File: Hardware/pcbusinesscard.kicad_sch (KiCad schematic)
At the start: 73 parts, among them J1 Conn_01x04_Pin, J10 USB_C_Receptacle_USB2.0, J2 Micro_SD_Card, J3 Conn_01x04_Pin, J4 Conn_01x03, SW1 ESC, SW2 `, SW3 1, SW4 2, SW98 SW_Push, U1 nRF52840, U2 24AA025E-OT, U3 24AA025E-OT, U4 24AA025E-OT, U5 BQ24090DGQ, Y1 32.768kHz, Y3 32Mhz

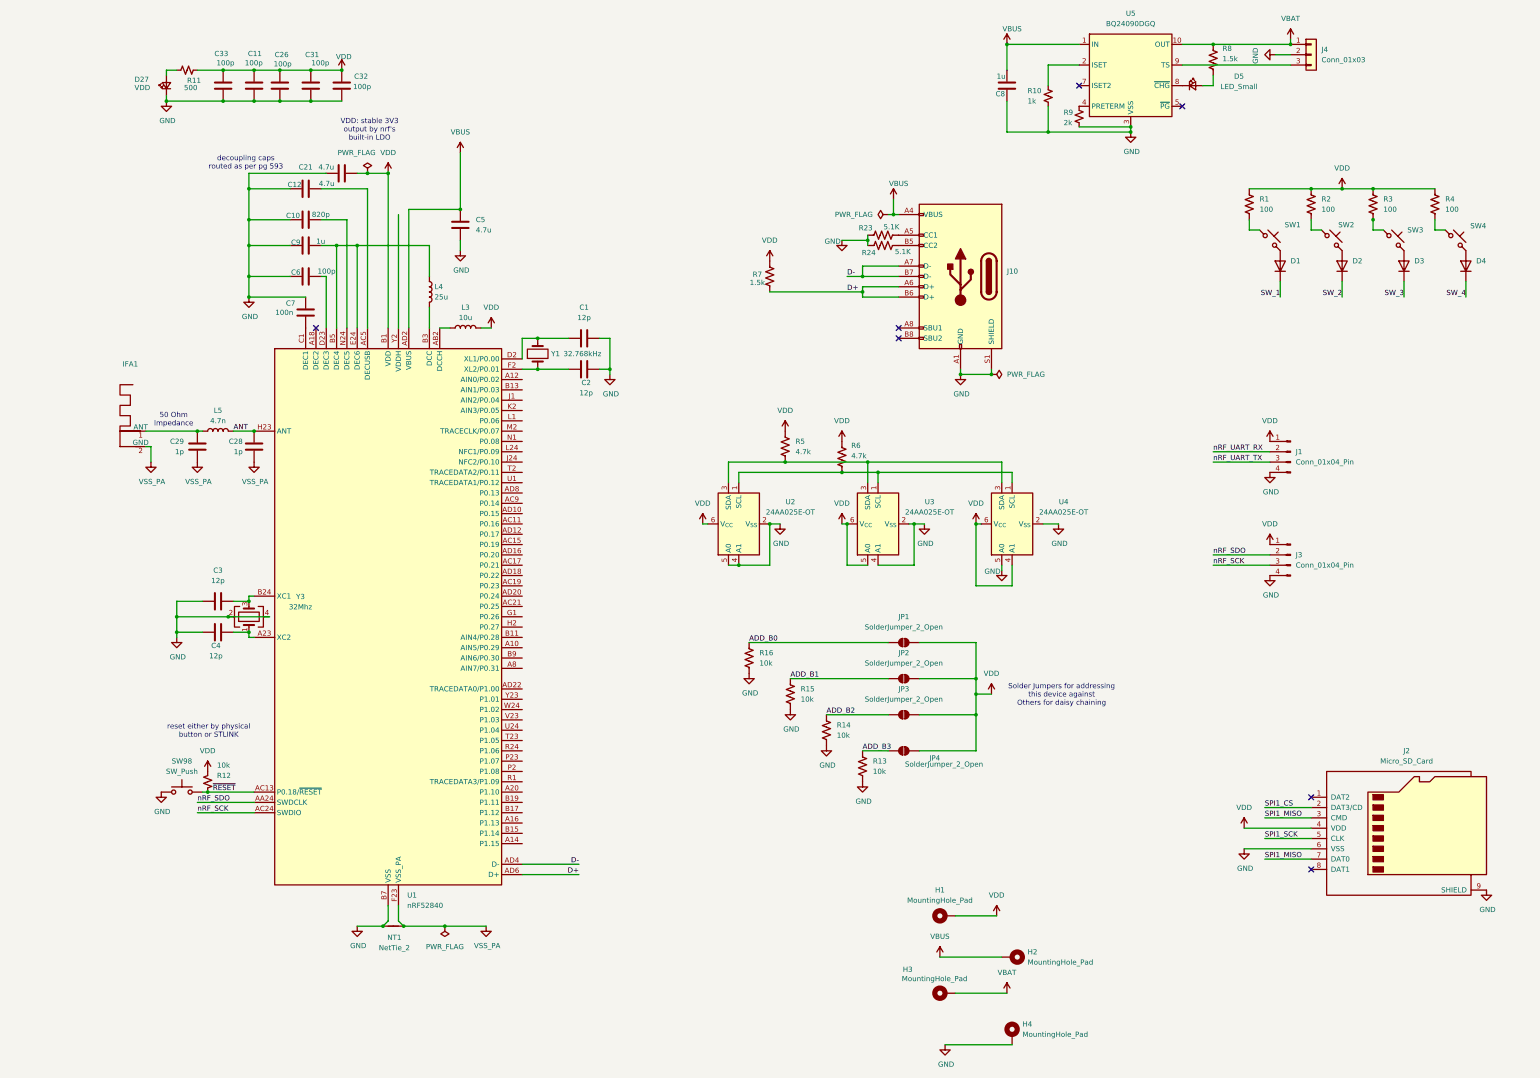
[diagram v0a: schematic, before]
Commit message: Overhaul entire design with RP2040
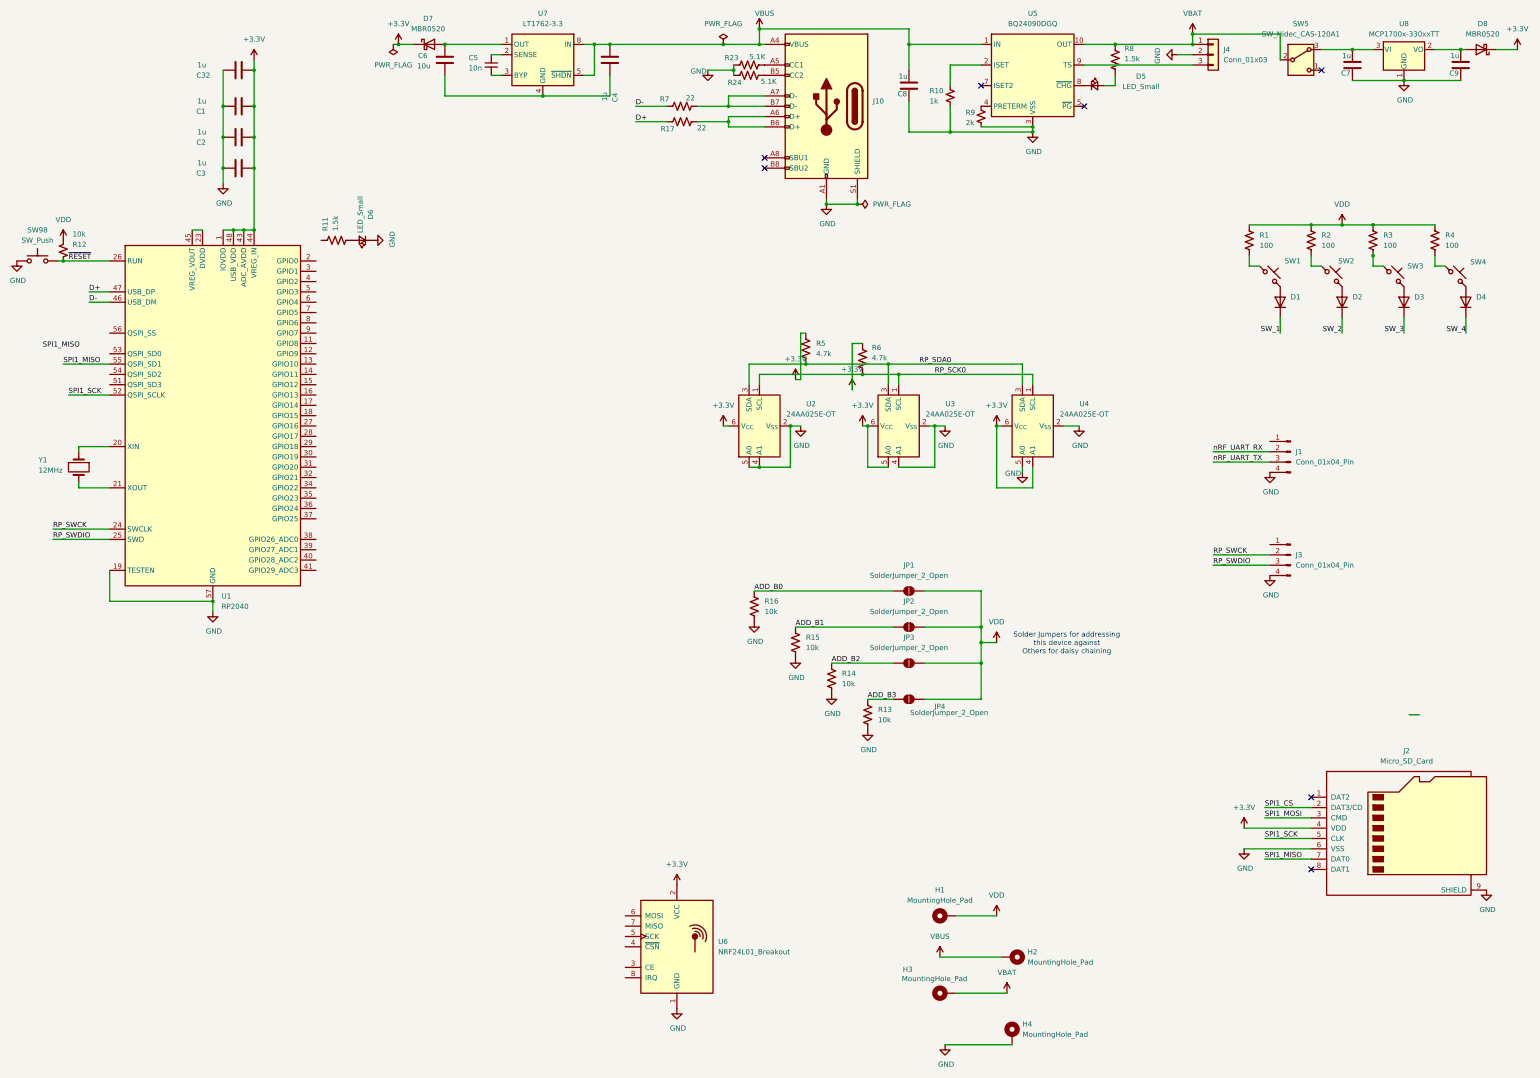
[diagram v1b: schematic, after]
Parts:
- removed C10: 820p, Capacitor_SMD:C_0603_1608Metric, symbol Device:C
- removed C11, C26, C31, C33: 100p, Capacitor_SMD:C_0603_1608Metric, symbol Device:C
- removed C12, C21, C5: 4.7u, Capacitor_SMD:C_0805_2012Metric, symbol Device:C
- removed C28, C29: 1p, Capacitor_SMD:C_0402_1005Metric, symbol Device:C
- removed D27: VDD, LED_SMD:LED_0402_1005Metric, symbol Device:LED_Small
- removed IFA1: ~, RF_Antenna:Texas_SWRA117D_2.4GHz_Right, symbol Custom_sym:IFA
- removed L3: 10u, Inductor_SMD:L_0402_1005Metric, symbol Device:L
- removed L4: 25u, Inductor_SMD:L_0402_1005Metric, symbol Device:L
- removed L5: 4.7n, Inductor_SMD:L_0402_1005Metric, symbol Device:L
- removed NT1: NetTie_2, NetTie:NetTie-2_SMD_Pad2.0mm, symbol Device:NetTie_2
- removed R11: 500, Resistor_SMD:R_0603_1608Metric, symbol Device:R_Small_US
- removed U1: nRF52840, Package_DFN_QFN:Nordic_AQFN-73-1EP_7x7mm_P0.5mm, symbol MCU_Nordic:nRF52840
- removed Y3: 32Mhz, Crystal:Crystal_SMD_2016-4Pin_2.0x1.6mm, symbol Device:Crystal_GND24
- added C5: 10n, Capacitor_SMD:C_0603_1608Metric, symbol Device:C_Small
- added D6: LED_Small, LED_THT:LED_D5.0mm, symbol Device:LED_Small
- added D7, D8: MBR0520, Diode_SMD:D_SOD-123, symbol Diode:MBR0520
- added R11: 1.5k, Resistor_SMD:R_0603_1608Metric, symbol Device:R_US
- added R17: 22, Resistor_SMD:R_0603_1608Metric, symbol Device:R_US
- added SW5: SW_Nidec_CAS-120A1, Button_Switch_SMD:Nidec_Copal_CAS-120A, symbol Switch:SW_Nidec_CAS-120A1
- added U1: RP2040, Package_DFN_QFN:QFN-56-1EP_7x7mm_P0.4mm_EP3.2x3.2mm, symbol MCU_RaspberryPi:RP2040
- added U6: NRF24L01_Breakout, RF_Module:nRF24L01_Breakout, symbol RF:NRF24L01_Breakout
- added U7: LT1762-3.3, Package_SO:MSOP-8_3x3mm_P0.65mm, symbol Regulator_Linear:LT1762-3.3
- added U8: MCP1700x-330xxTT, Package_TO_SOT_SMD:SOT-23, symbol Regulator_Linear:MCP1700x-330xxTT
- C1, C2, C3, C4: value 12p -> 1u; footprint Capacitor_SMD:C_0402_1005Metric -> Capacitor_SMD:C_0603_1608Metric; LCSC C1547 -> C14858
- C32: value 100p -> 1u
- C6: value 100p -> 10u
- C7: value 100n -> 1u; LCSC C14663 -> C15849
- J1, J3: footprint Connector_Card:microSD_HC_Molex_47219-2001 -> Connector_JST:JST_PH_B4B-PH-K_1x04_P2.00mm_Vertical
- R7: value 1.5k -> 22; LCSC C22843 -> C23186
- SW1, SW2, SW3, SW4: footprint ScottoKeebs_Hotswap:Hotswap_MX_1.00u -> ScottoKeebs_MX:MX_PCB_1.00u
- Y1: value 32.768kHz -> 12MHz; footprint Crystal:Crystal_SMD_3215-2Pin_3.2x1.5mm -> Crystal:Crystal_SMD_5032-2Pin_5.0x3.2mm; LCSC C32346 -> (none)
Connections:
- net D+: now also R17.1, U1.47 (USB_DP); no longer J10.A6 (D+), J10.B6 (D+), R7.2
- net D-: now also R7.1, U1.46 (USB_DM); no longer J10.A7 (D-), J10.B7 (D-)
- net GND: now also C32.1, D6.1 (K), U1.19 (TESTEN), U1.57 (GND), U6.1 (GND), U8.1 (GND); no longer C32.2, C4.1, C6.2
- net SPI1_MISO: now also U1.55 (QSPI_SD1); no longer J2.3 (CMD)
- net SPI1_SCK: now also U1.52 (QSPI_SCLK)
- net VBAT: now also SW5.2 (B)
- net VBUS: now also C4.2, U7.5 (~{SHDN}), U7.8 (IN)
- net VDD: no longer C32.1, J1.1 (Pin_1), J2.4 (VDD), J3.1 (Pin_1), R5.1, R6.1, R7.1, U2.6 (V_{CC}), U3.5 (A0), U3.6 (V_{CC}), U4.4 (A1), U4.6 (V_{CC})
- net ~{RESET}: now also U1.26 (RUN)
- net +3.3V: now reaches C3.2
- net +3.3V: now also C1.2, C2.2, C32.2, J2.4 (VDD), R5.1, R6.1, U2.6 (V_{CC}), U3.5 (A0), U3.6 (V_{CC}), U4.4 (A1), U4.6 (V_{CC}), D7.1 (K), D8.1 (K), U1.1 (IOVDD), U1.10 (IOVDD), U1.22 (IOVDD), U1.33 (IOVDD), U1.42 (IOVDD), U1.43 (ADC_AVDD), U1.44 (VREG_IN), U1.48 (USB_VDD), U1.49 (IOVDD), U6.2 (VCC)
- net RP_SDA0: now reaches R5.2, U2.3 (SDA), U3.3 (SDA), U4.3 (SDA)
- net at C9.1: now also D8.2 (A), U8.2 (VO)
- net at C7.1: now also SW5.3 (A), U8.3 (VI)
- net at Y1.2: now also U1.21 (XOUT); no longer C1.2
- net at C6.1: now also C4.1, U7.4 (GND)
- net at Y1.1: now also U1.20 (XIN); no longer C2.2
- net RP_SCK0: now reaches R6.2, U2.1 (SCL), U3.1 (SCL), U4.1 (SCL)
- net nRF_SCK renamed RP_SWDIO
- net RP_SWDIO: now also U1.25 (SWD)
- net nRF_SDO renamed RP_SWCK
- net RP_SWCK: now also U1.24 (SWCLK)
- new net: C6.2, D7.2 (A), U7.1 (OUT)
- new net: C5.1, U7.2 (SENSE)
- new net: C5.2, U7.3 (BYP)
- new net: D6.2 (A), R11.2
- new net: U1.23 (DVDD), U1.45 (VREG_VOUT), U1.50 (DVDD)
- new net: J10.A7 (D-), J10.B7 (D-), R7.2
- new net: J10.A6 (D+), J10.B6 (D+), R17.2
- new net SPI1_MOSI: J2.3 (CMD)
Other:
- note removed: "50 Ohm Impedance"
- note removed: "VDD: stable 3V3 output by nrf's built-in LDO"
- note removed: "decoupling caps routed as per pg 593"
- note removed: "reset either by physical button or STLINK"
- moved on the sheet: C32, C8, D1, D2, D3, D4, D5, J10, J4, JP1, JP2, JP3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

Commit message: adding to layout
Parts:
- added C10: 1u, Capacitor_SMD:C_0603_1608Metric, symbol Device:C
- added D10, D9: LED_Small, LED_SMD:LED_0805_2012Metric, symbol Device:LED_Small
- added R18, R19: 1.5k, Resistor_SMD:R_0603_1608Metric, symbol Device:R_US
- C1: value 1u -> 4.7u
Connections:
- net +3.3V: now also H3.1, J1.1 (Pin_1), J3.1 (Pin_1), JP1.2 (B), JP2.2 (B), JP3.2 (B), JP4.2 (B), R1.1, R12.1, R2.1, R3.1, R4.1, C10.2
- net ADD_B0: now also U1.40 (GPIO28_ADC2)
- net ADD_B1: now also U1.39 (GPIO27_ADC1)
- net ADD_B2: now also U1.38 (GPIO26_ADC0)
- net ADD_B3: now also U1.37 (GPIO25)
- net GND: now also C10.1, D10.1 (K), D9.1 (K)
- net RP_SCK0: now also U1.29 (GPIO18)
- net RP_SDA0: now also U1.30 (GPIO19)
- net SPI1_CS: now also U1.12 (GPIO9)
- net SPI1_MISO: now also U1.15 (GPIO12); no longer U1.55 (QSPI_SD1)
- net SPI1_MOSI: now also U1.9 (GPIO7)
- net SPI1_SCK: now also U1.13 (GPIO10); no longer U1.52 (QSPI_SCLK)
- net SW_1: now also U1.34 (GPIO22)
- net SW_2: now also U1.36 (GPIO24)
- net SW_3: now also U1.31 (GPIO20)
- net SW_4: now also U1.35 (GPIO23)
- net VBAT: now also H2.1; no longer H3.1
- net VBUS: now also H1.1, R11.1; no longer H2.1
- net d-: now reaches J10.A7 (D-), J10.B7 (D-), R7.2
- net d+: now reaches J10.A6 (D+), J10.B6 (D+), R17.2
- removed net VDD: H1.1, JP1.2 (B), JP2.2 (B), JP3.2 (B), JP4.2 (B), R1.1, R12.1, R2.1, R3.1, R4.1
- new net: D9.2 (A), R18.2
- new net: D10.2 (A), R19.2
- no-connect marks 7 -> 8
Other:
- note added: "MCU"
- note added: "POWER"
- note removed: "Solder Jumpers for addressing this device against Others for daisy chaining"
- moved on the sheet: C1, C2, C3, C32, C4, C5, C6, C7, C8, C9, D1, D2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

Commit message: Finish Draft
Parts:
- removed D7, D8: MBR0520, Diode_SMD:D_SOD-123, symbol Diode:MBR0520
- added C11: 1u, Capacitor_SMD:C_0603_1608Metric, symbol Device:C
- added J5: Conn_ST_STDC14, Connector_PinHeader_1.27mm:PinHeader_2x07_P1.27mm_Vertical, symbol Connector:Conn_ST_STDC14
- added R20: 1.5k, Resistor_SMD:R_0603_1608Metric, symbol Device:R_US
- added R21, R22: 10k, Resistor_SMD:R_0603_1608Metric, symbol Device:R_US
- added TP1, TP2, TP3, TP4, TP5: TestPoint, TestPoint:TestPoint_Keystone_5010-5014_Multipurpose, symbol Connector:TestPoint
- added U9: TPS2116DRL, Package_TO_SOT_SMD:SOT-583-8, symbol Power_Management:TPS2116DRL
- J3: footprint Connector_JST:JST_PH_B4B-PH-K_1x04_P2.00mm_Vertical -> Connector_PinHeader_2.54mm:PinHeader_1x04_P2.54mm_Vertical
- J4: footprint Connector_JST:JST_GH_SM03B-GHS-TB_1x03-1MP_P1.25mm_Horizontal -> Connector_JST:JST_ZH_B3B-ZR_1x03_P1.50mm_Vertical
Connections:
- net +3.3V: now also C11.2, J5.3 (VCC), U9.2 (VOUT), U9.7 (VOUT)
- net GND: now also C4.1, C6.1, U7.4 (GND), C11.1, J5.11 (GNDDetect), J5.5 (GND), J5.7 (GND), R21.2, U9.1 (GND)
- net RP_SCK0: now also TP2.1
- net RP_SDA0: now also TP1.1
- net RP_SWCK: now also J5.6 (JCLK/SWCLK)
- net RP_SWDIO: now also J5.4 (JTMS/SWDIO)
- net SPI1_MISO: now also TP4.1
- net SPI1_MOSI: now also TP5.1
- net SPI1_SCK: now also TP3.1
- net VBAT: now also SW5.1 (C), R22.2
- net nRF_UART_RX: now also J1.3 (Pin_3), U1.28 (GPIO17); no longer J1.2 (Pin_2)
- net nRF_UART_TX: now also J1.2 (Pin_2), U1.27 (GPIO16); no longer J1.3 (Pin_3)
- net ~{RESET}: now also J5.12 (~{RST})
- net VBUS_LDO: now reaches C6.2, U7.1 (OUT)
- net VBUS_LDO: now also R20.1, U9.3 (VIN1), U9.4 (PR1), U9.5 (MODE)
- net status_LED0: now reaches R18.1
- net status_LED0: now also U1.51 (QSPI_SD3)
- net nRF_CE: now reaches U6.3 (CE)
- net nRF_CE: now also U1.2 (GPIO0)
- net SPI0_CSN: now reaches U6.4 (~{CSN})
- net SPI0_CSN: now also U1.3 (GPIO1)
- net SPI0_SCK: now reaches U6.5 (SCK)
- net SPI0_SCK: now also U1.4 (GPIO2)
- net SPI0_MOSI: now reaches U6.6 (MOSI)
- net SPI0_MOSI: now also U1.5 (GPIO3)
- net SPI0_MISO: now reaches U6.7 (MISO)
- net SPI0_MISO: now also U1.6 (GPIO4)
- net nRF_IRQ: now reaches U6.8 (IRQ)
- net nRF_IRQ: now also U1.7 (GPIO5)
- net status_LED1: now reaches R19.1
- net status_LED1: now also U1.52 (QSPI_SCLK)
- net at U1.41 (GPIO29_ADC3): now also R21.1, R22.1
- net VBAT_LDO: now reaches C9.1, U8.2 (VO)
- net VBAT_LDO: now also U9.6 (VIN2)
- new net: R20.2, U9.8 (ST)
- no-connect marks 8 -> 22
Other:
- note added: "redundant header"
- moved on the sheet: C1, C10, C2, C3, C32, C7, C9, D1, D10, D2, D3, D4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

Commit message: Finish first draft of routing
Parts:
- removed D1: ESC, ScottoKeebs_Components:Diode_SOD-123, symbol Device:D
- removed D2: ~/`, ScottoKeebs_Components:Diode_SOD-123, symbol Device:D
- removed D3: 1, ScottoKeebs_Components:Diode_SOD-123, symbol Device:D
- removed D4: 2, ScottoKeebs_Components:Diode_SOD-123, symbol Device:D
- removed J1: Conn_01x04_Pin, Connector_JST:JST_PH_B4B-PH-K_1x04_P2.00mm_Vertical, symbol Connector:Conn_01x04_Pin
- removed J3: Conn_01x04_Pin, Connector_PinHeader_2.54mm:PinHeader_1x04_P2.54mm_Vertical, symbol Connector:Conn_01x04_Pin
- removed R19: 1.5k, Resistor_SMD:R_0603_1608Metric, symbol Device:R_US
- removed R2: 100, Resistor_SMD:R_0402_1005Metric, symbol Device:R_US
- removed SW2: `, ScottoKeebs_MX:MX_PCB_1.00u, symbol Switch:SW_Push_45deg
- removed U6: NRF24L01_Breakout, RF_Module:nRF24L01_Breakout, symbol RF:NRF24L01_Breakout
- removed U7: LT1762-3.3, Package_SO:MSOP-8_3x3mm_P0.65mm, symbol Regulator_Linear:LT1762-3.3
- added C12, C13: 22p, Capacitor_SMD:C_0402_1005Metric, symbol Device:C_Small
- added C14: 33nF, Capacitor_SMD:C_0402_1005Metric, symbol Device:C_Small
- added C15: 1n, Capacitor_SMD:C_0402_1005Metric, symbol Device:C_Small
- added C16: 10n, Capacitor_SMD:C_0402_1005Metric, symbol Device:C_Small
- added C17, C18: 1p, Capacitor_SMD:C_0402_1005Metric, symbol Device:C_Small
- added D1: SS34, Diode_SMD:D_SMA, symbol Diode:SS34
- added D11, D12, D8: LED_Small, LED_SMD:LED_0805_2012Metric, symbol Device:LED_Small
- added IFA1: ~, RF_Antenna:Texas_SWRA117D_2.4GHz_Right, symbol Custom_sym:IFA
- added J6, J7: Conn_01x04_Pin, Connector_JST:JST_PH_B4B-PH-K_1x04_P2.00mm_Vertical, symbol Connector:Conn_01x04_Pin
- added L1: 3.9n, Inductor_SMD:L_0402_1005Metric, symbol Device:L
- added L2: 33u, Inductor_SMD:L_0402_1005Metric, symbol Device:L
- added L3: 8.2n, Inductor_SMD:L_0402_1005Metric, symbol Device:L_Small
- added L4: 2.7n, Inductor_SMD:L_0402_1005Metric, symbol Device:L_Small
- added Q1, Q2, Q3, Q4, Q5: MMBT3904, Package_TO_SOT_SMD:SOT-23, symbol Transistor_BJT:MMBT3904
- added R19, R26: 1300, Resistor_SMD:R_0402_1005Metric, symbol Device:R_Small_US
- added R25: 22k, Resistor_SMD:R_0603_1608Metric, symbol Device:R_US
- added R27, R28, R29: 1.3k, Resistor_SMD:R_0402_1005Metric, symbol Device:R_Small_US
- added R30, R31, R32, R33: 400, Resistor_SMD:R_0402_1005Metric, symbol Device:R_US
- added U10: NRF24L01, Package_DFN_QFN:QFN-20-1EP_4x4mm_P0.5mm_EP2.5x2.5mm, symbol RF:NRF24L01
- added U12: LM2596S-3.3, Package_TO_SOT_SMD:TO-263-5_TabPin3, symbol Regulator_Switching:LM2596S-3.3
- added Y2: Crystal, Crystal:Crystal_SMD_HC49-SD, symbol Device:Crystal
- C5: value 10n -> 4.7pF; footprint Capacitor_SMD:C_0603_1608Metric -> Capacitor_SMD:C_0402_1005Metric
- J5: footprint Connector_PinHeader_1.27mm:PinHeader_2x07_P1.27mm_Vertical -> Connector:Tag-Connect_TC2070-IDC-FP_2x07_P1.27mm_Vertical
- R18: value 1.5k -> 400; footprint Resistor_SMD:R_0603_1608Metric -> Resistor_SMD:R_0402_1005Metric
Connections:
- net nRF_UART_RX is gone; now on net RP_UART_RX: U1.28 (GPIO17)
- net nRF_UART_TX is gone; now on net RP_UART_TX: U1.27 (GPIO16)
- net +3.3V: now also R18.1, C15.2, C16.2, J6.1 (Pin_1), J7.1 (Pin_1), R30.1, R31.1, R32.1, R33.1, U10.15 (VDD), U10.18 (VDD), U10.7 (VDD)
- net GND: now also C5.1, C12.2, C13.2, C14.1, C15.1, C16.1, C18.1, D1.2 (A), J6.4 (Pin_4), J7.4 (Pin_4), L4.2, Q1.2 (E), Q2.2 (E), Q3.2 (E), Q4.2 (E), Q5.2 (E), R25.2, U10.14 (VSS), U10.17 (VSS), U10.20 (VSS), U10.8 (VSS), U12.3 (GND), U12.5 (~{ON}/OFF); no longer D10.1 (K), D9.1 (K)
- net SPI0_CSN: now also U10.2 (CSN)
- net SPI0_MISO: now also U1.2 (GPIO0), U10.5 (MISO); no longer U1.6 (GPIO4)
- net SPI0_MOSI: now also U10.4 (MOSI)
- net SPI0_SCK: now also U1.8 (GPIO6), U10.3 (SCK); no longer U1.4 (GPIO2)
- net SW_1: now also SW1.2, U1.32 (GPIO21); no longer U1.34 (GPIO22)
- net SW_3: now also SW3.2
- net SW_4: now also SW4.2, U1.34 (GPIO22); no longer U1.35 (GPIO23)
- net VBUS: now also U12.1 (VIN)
- net VBUS_LDO: no longer C6.2, U9.3 (VIN1), U9.4 (PR1), U9.5 (MODE)
- net nRF_CE: now also U1.7 (GPIO5), U10.1 (CE); no longer U1.2 (GPIO0)
- net nRF_IRQ: now also U1.4 (GPIO2), U10.6 (IRQ); no longer U1.7 (GPIO5)
- net at C5.2: now also IFA1.2 (GND), U10.11 (VDD_PA)
- net at R18.2: now also D11.2 (A); no longer D9.2 (A)
- net at D10.2 (A): now also R33.2
- net LED_4: now reaches U1.53 (QSPI_SD0)
- net LED_4: now also R26.1
- net LED_2: now reaches U1.54 (QSPI_SD2)
- net LED_2: now also R27.1
- net LED_3: now reaches U1.55 (QSPI_SD1)
- net LED_3: now also R29.1
- net RP_UART_RX: now reaches J5.13 (VCP_RX)
- net RP_UART_TX: now reaches J5.14 (VCP_TX)
- net RP_SCK0 renamed RP_I2C0_SDA
- net RP_SDA0 renamed RP_I2C0_SCK
- net SW_2 renamed RP_I2C1_SCL
- net RP_I2C1_SCL: now also J6.3 (Pin_3), J7.3 (Pin_3)
- net VBAT_LDO renamed VBAT_REG
- net status_LED0 renamed LED_1
- net LED_1: now also R19.1; no longer R18.1
- net status_LED1 renamed LED_0
- net LED_0: now also R28.1
- new net: L2.2, U12.2 (OUT)
- new net: R25.1, U10.16 (IREF)
- new net: Q4.1 (B), R28.2
- new net: Q1.1 (B), R19.2
- new net: D12.1 (K), Q1.3 (C)
- new net: C13.1, U10.9 (XC2), Y2.1
- new net: L3.1, L4.1, U10.12 (ANT1)
- new net: Q5.1 (B), R27.2
- new net: D12.2 (A), R30.2
- new net: C12.1, U10.10 (XC1), Y2.2
- new net: Q3.1 (B), R29.2
- new net: D8.1 (K), Q3.3 (C)
- new net: D9.1 (K), Q4.3 (C)
- new net: Q2.1 (B), R26.2
- new net: D11.1 (K), Q2.3 (C)
- new net: C17.2, C18.2, IFA1.1 (ANT)
- new net: C14.2, U10.19 (DVDD)
- new net: L1.1, U10.13 (ANT2)
- new net: C17.1, L1.2, L3.2
- new net: D9.2 (A), R32.2
- new net: D10.1 (K), Q5.3 (C)
- new net: D8.2 (A), R31.2
- new net RP_I2C1_SDA: J6.2 (Pin_2), J7.2 (Pin_2), U1.35 (GPIO23)
- new net VBUS_REG: C6.2, D1.1 (K), L2.1, U12.4 (FB), U9.3 (VIN1), U9.4 (PR1), U9.5 (MODE)
- no-connect marks 22 -> 14
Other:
- note removed: "redundant header"
- company: (none) -> Aryan Ghosh
- title: (none) -> PCBusiness Card
- moved on the sheet: C1, C10, C11, C2, C3, C32, C4, C6, C7, C8, C9, D10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

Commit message: dont remember
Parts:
- J2: LCSC (none) -> C164170
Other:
- moved on the sheet: J5, R20, U9

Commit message: Fixed DRC and cleaned up schematic
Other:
- note added: "2.4Ghz"
- note added: "EEPROM"
- note added: "I2C Daisy Chain"
- note added: "LEDs"
- note added: "SD CARD"
- note added: "SWD + GPIO"
- moved on the sheet: C1, C10, C2, C32, H1, H2, H3, H4, J5, J6, J7, JP1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
